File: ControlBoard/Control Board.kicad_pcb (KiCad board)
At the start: 2 copper layers, 120.7 x 77.5 mm, 57 parts, among them J1 Conn_01x02_Pin, Q1 BSS138, U1 SN74LVC245APW, U2 ULN2003

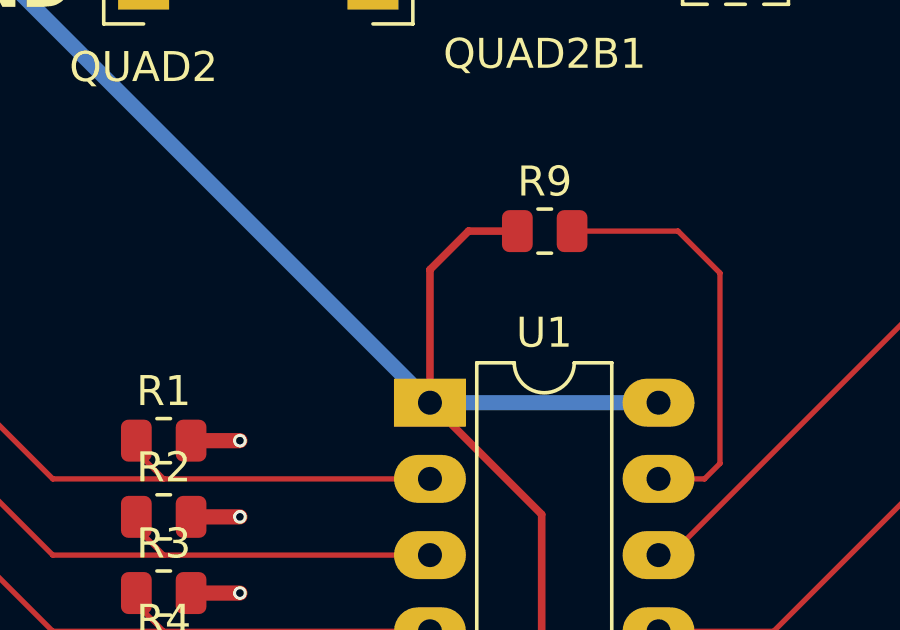
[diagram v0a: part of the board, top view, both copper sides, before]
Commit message: Chassis driving
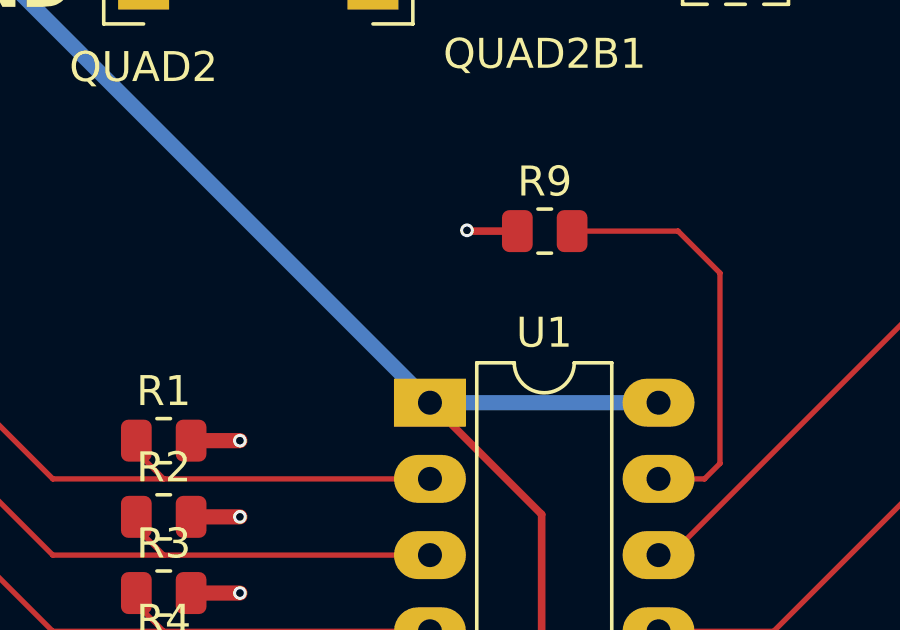
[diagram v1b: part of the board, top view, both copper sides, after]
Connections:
- R9 pad 1: +3V3 -> GND
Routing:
- net +3V3: track 208.2 -> 200.3 mm
- net GND: track 134.3 -> 135.9 mm, vias 16 -> 17
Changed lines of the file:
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@@
 		(tags "diode")
 		(property "Reference" "D1"
-			(at 3.2004 -1.778 360)
+			(at 3.2004 -1.778 0)
 			(layer "F.SilkS")
 			(effects
@@
 		)
 		(property "Value" "D"
-			(at 0 1.82 360)
+			(at 0 1.82 0)
 			(layer "F.Fab")
 			(hide yes)
@@
 			(layers "F.Cu" "F.Paste" "F.Mask")
 			(roundrect_rratio 0.243902)
-			(net 27 "+3V3")
+			(net 14 "GND")
 			(pintype "passive")
 		)
@@
 		(tags "diode handsolder")
 		(property "Reference" "D2"
-			(at 0 -1.65 360)
+			(at 0 -1.65 0)
 			(layer "F.SilkS")
 			(hide yes)
@@
 		)
 		(property "Value" "D"
-			(at 3.302 1.0668 360)
+			(at 3.302 1.0668 0)
 			(layer "F.Fab")
 			(hide yes)
@@
 		(fp_arc
 			(start -0.7 1)
-			(mid -1.19498 0.79498)
+			(mid -1.194981 0.79498)
 			(end -1.4 0.300001)
 			(stroke
@@
 	)
 	(segment
+		(start 128.27 94.615)
+		(end 128.2446 94.615)
+		(width 0.254)
+		(layer "F.Cu")
+		(net 14)
+	)
+	(segment
 		(start 160.035 86.36)
 		(end 160.035 81.28)
@@
 	)
 	(segment
+		(start 128.2446 94.615)
+		(end 128.2192 94.5896)
+		(width 0.254)
+		(layer "F.Cu")
+		(net 14)
+	)
+	(segment
 		(start 160.02 73.66)
 		(end 160.02 68.58)
@@
 	)
 	(segment
+		(start 128.27 94.615)
+		(end 129.8975 94.615)
+		(width 0.254)
+		(layer "F.Cu")
+		(net 14)
+	)
+	(segment
 		(start 160.02 123.205)
 		(end 160.035 123.19)
@@
 	)
 	(via
+		(at 128.2192 94.5896)
+		(size 0.4572)
+		(drill 0.254)
+		(layers "F.Cu" "B.Cu")
+		(net 14)
+	)
+	(via
 		(at 64.8716 86.0044)
 		(size 0.4572)
@@
 	)
 	(segment
-		(start 126.985 95.9)
-		(end 128.27 94.615)
-		(width 0.254)
-		(layer "F.Cu")
-		(net 27)
-	)
-	(segment
 		(start 128.6764 129.032)
 		(end 116.4844 129.032)
@@
 		(layer "F.Cu")
 		(net 27)
-	)
-	(segment
-		(start 126.985 100.335)
-		(end 126.985 95.9)
-		(width 0.254)
-		(layer "F.Cu")
-		(net 27)
-	)
-	(segment
-		(start 128.27 94.615)
-		(end 129.8975 94.615)
-		(width 0.254)
-		(layer "F.Cu")
-		(net 27)
